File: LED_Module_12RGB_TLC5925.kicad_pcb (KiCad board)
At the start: 2 copper layers, 150 x 42 mm, 33 parts, among them J1 Conn_01x02_Pin, J2 Conn_02x05_Counter_Clockwise, J3 Conn_02x05_Counter_Clockwise, U1 TLC5925IPWR, U2 AMS1117-3.3

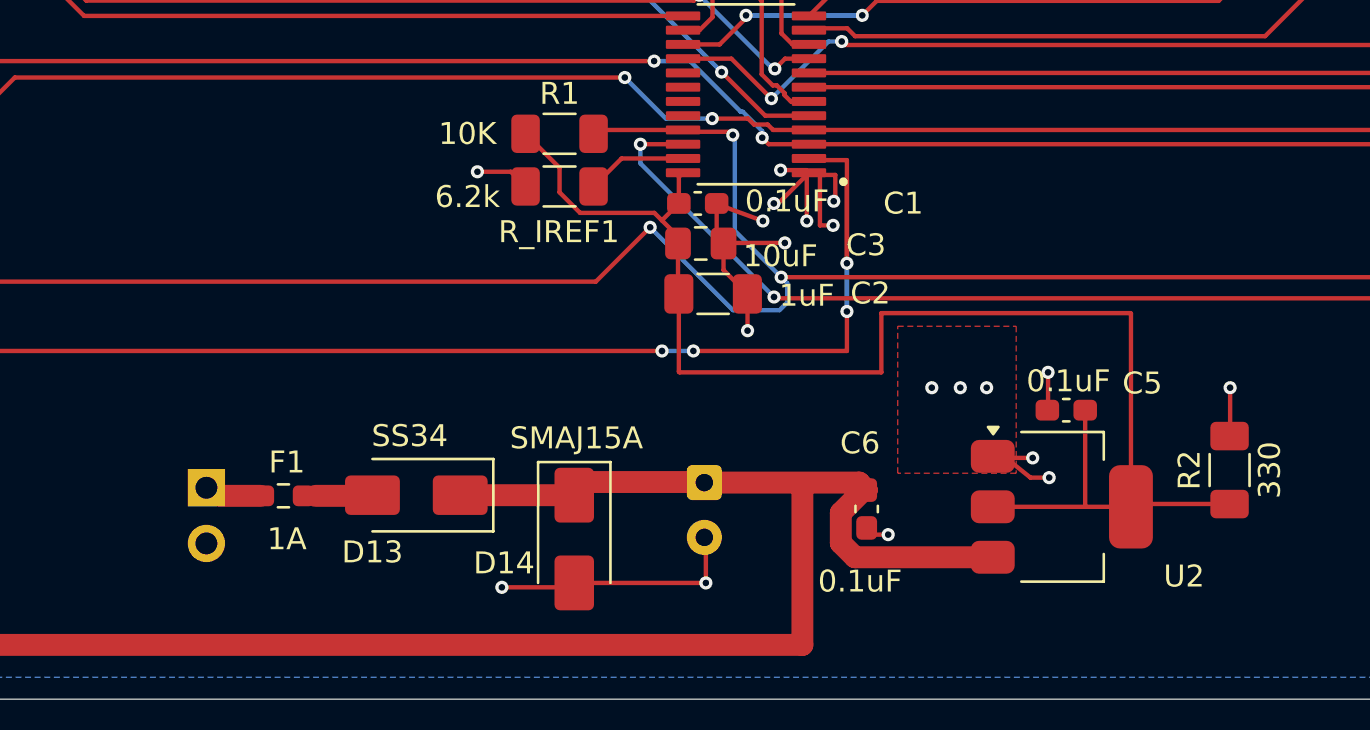
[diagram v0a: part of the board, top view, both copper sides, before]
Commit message: improved trace size and vias
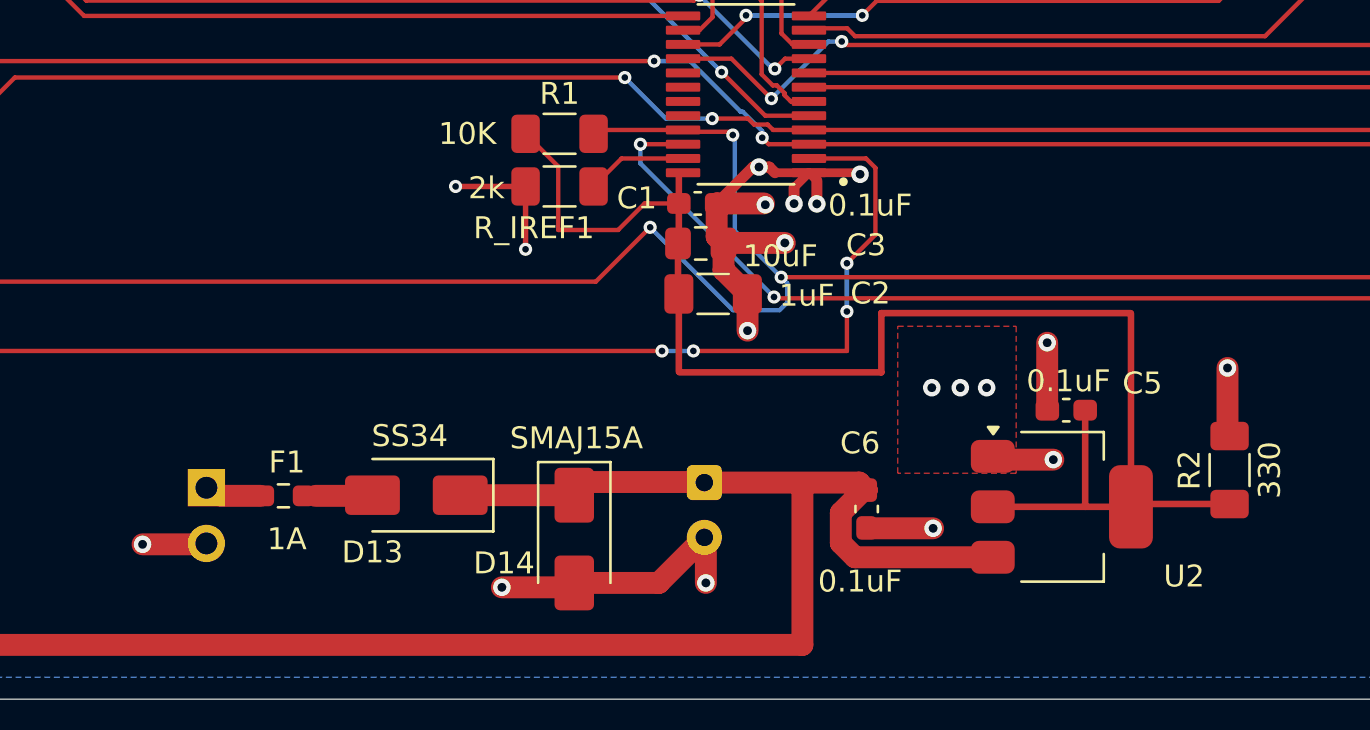
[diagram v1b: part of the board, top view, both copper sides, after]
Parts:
- R_IREF1: value 6.2k -> 2k
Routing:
- net GND: track 10.9 -> 30.4 mm
- net SDI: track 5.98 -> 10.3 mm
- net VDD_3V3: track 60.8 -> 62.9 mm
